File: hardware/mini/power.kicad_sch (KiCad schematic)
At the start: 33 parts, among them U1 TPS55289

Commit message: mini
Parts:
- added J2: USB_C_Receptacle_USB2.0_16P, symbol Connector:USB_C_Receptacle_USB2.0_16P
- added U7: CH224K, Package_SO:SSOP-10-1EP_3.9x4.9mm_P1mm_EP2.1x3.3mm, symbol Interface_USB:CH224K
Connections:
- new net: J2.A1 (GND), J2.A12 (GND), J2.B1 (GND), J2.B12 (GND)
- new net: J2.A4 (VBUS), J2.A9 (VBUS), J2.B4 (VBUS), J2.B9 (VBUS)
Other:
- moved on the sheet: C1, C10, C11, C12, C13, C14, C15, C16, C17, C18, C19, C2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

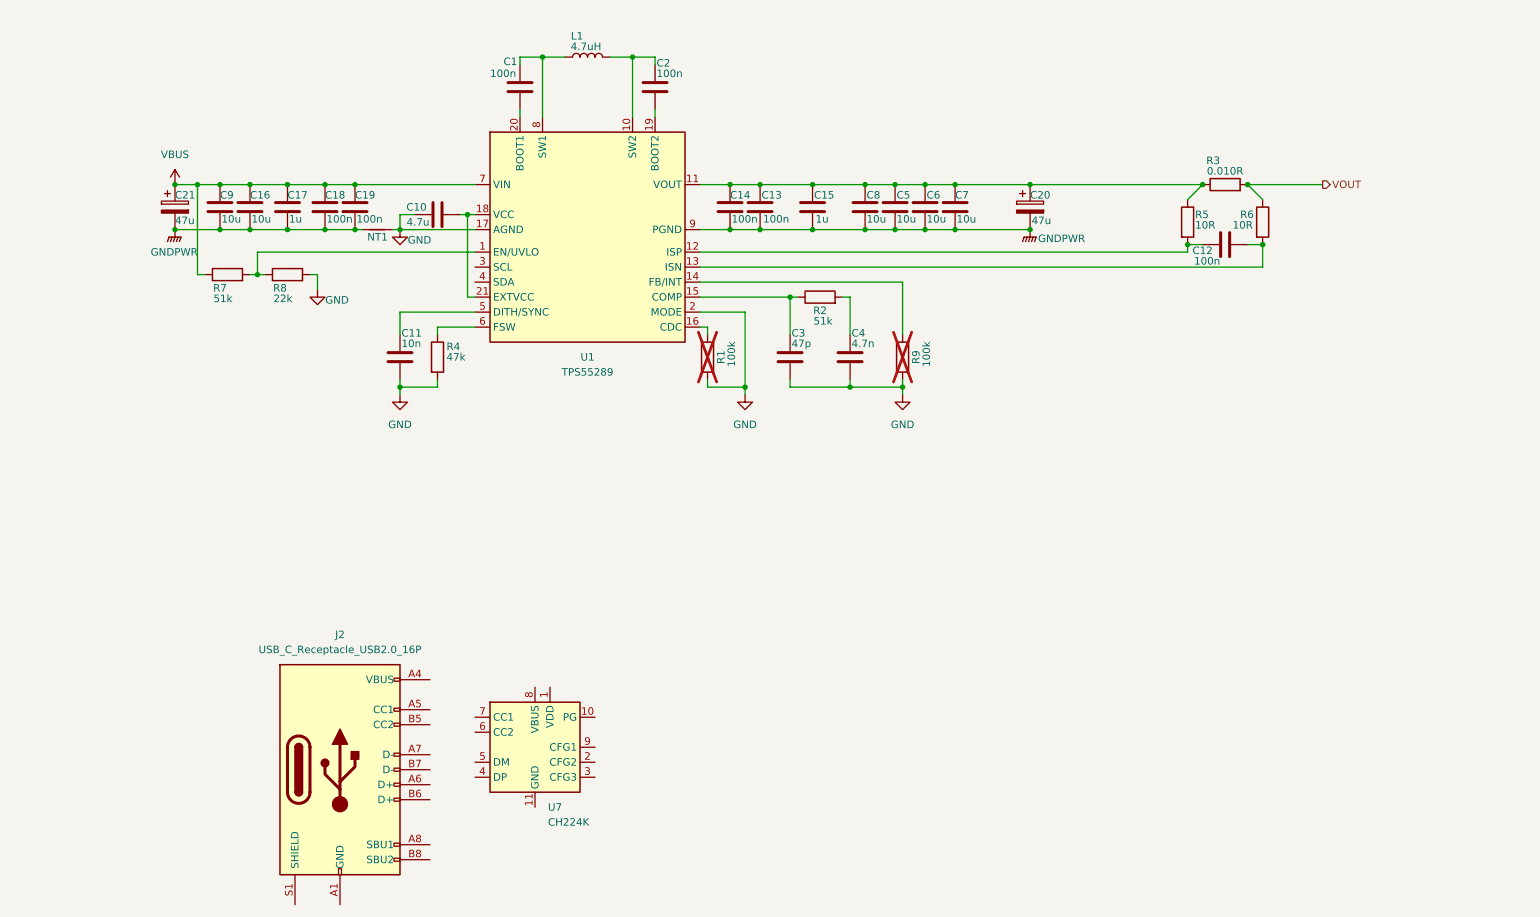
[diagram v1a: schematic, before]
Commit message: add interface & RP2040
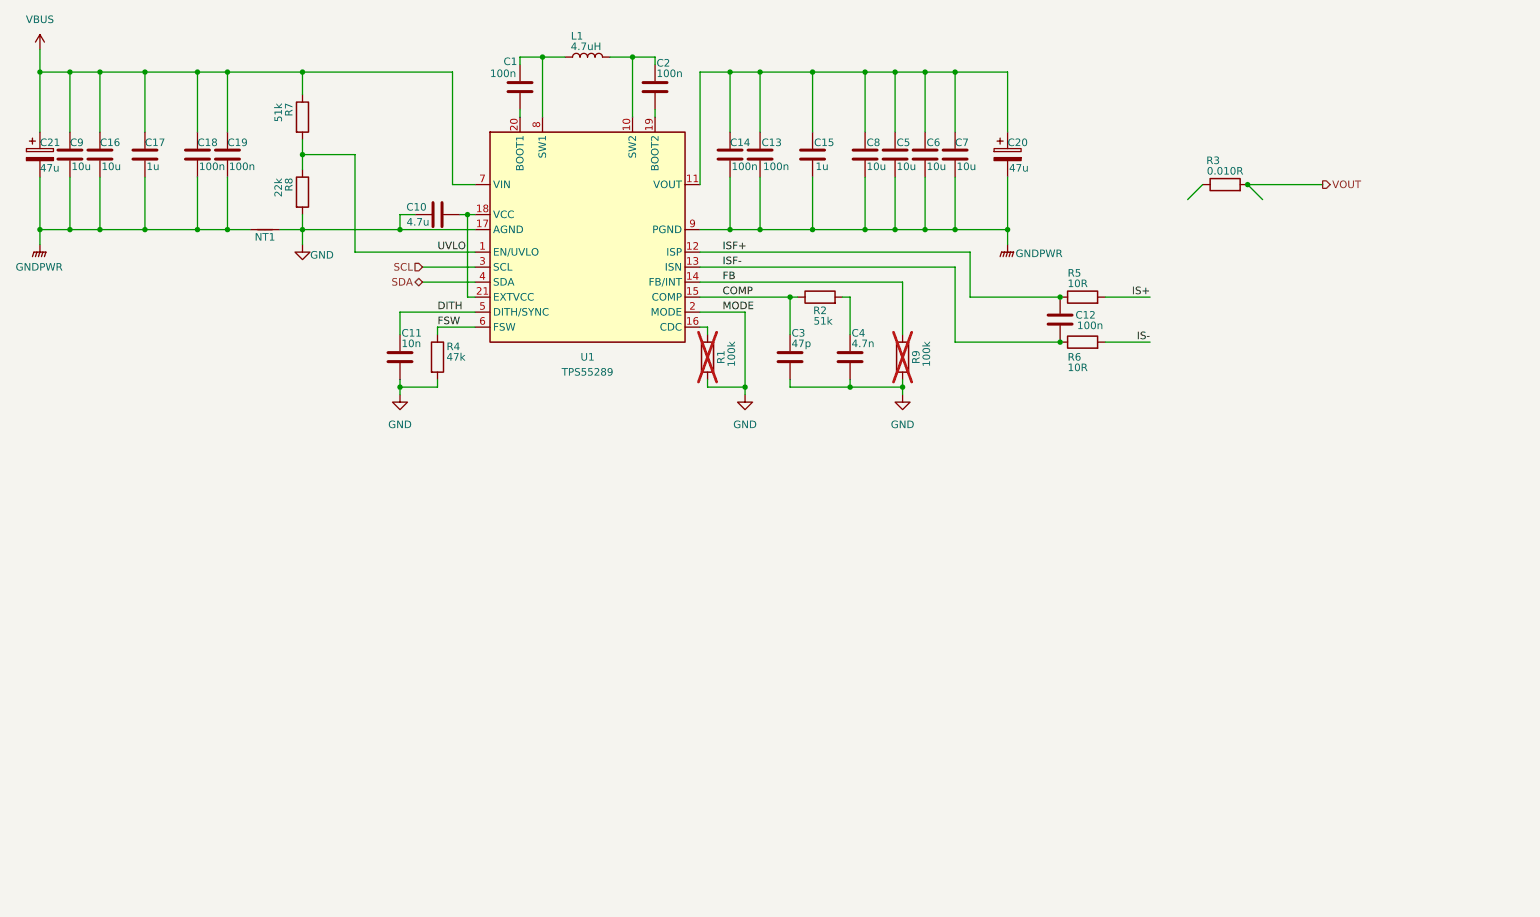
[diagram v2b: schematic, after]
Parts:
- removed J2: USB_C_Receptacle_USB2.0_16P, symbol Connector:USB_C_Receptacle_USB2.0_16P
- removed U7: CH224K, Package_SO:SSOP-10-1EP_3.9x4.9mm_P1mm_EP2.1x3.3mm, symbol Interface_USB:CH224K
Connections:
- net VOUT: no longer R6.1
- net UVLO: now reaches R7.2, R8.1, U1.1 (EN/UVLO)
- net at C13.1, C14.1, C15.1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: no longer R3.1, R5.1
- net FB: now reaches R9.2, U1.14 (FB/INT)
- net COMP: now reaches C3.1, R2.1, U1.15 (COMP)
- net SCL: now reaches U1.3 (SCL)
- net SDA: now reaches U1.4 (SDA)
- net DITH: now reaches C11.1, U1.5 (DITH/SYNC)
- net FSW: now reaches R4.1, U1.6 (FSW)
- new net IS+: R5.2
- new net IS-: R6.2
- new net ISF+: C12.2, R5.1, U1.12 (ISP)
- new net ISF-: C12.1, R6.1, U1.13 (ISN)
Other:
- moved on the sheet: C12, C13, C14, C15, C16, C17, C18, C19, C20, C21, C5, C6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

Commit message: finalize parts in schematic
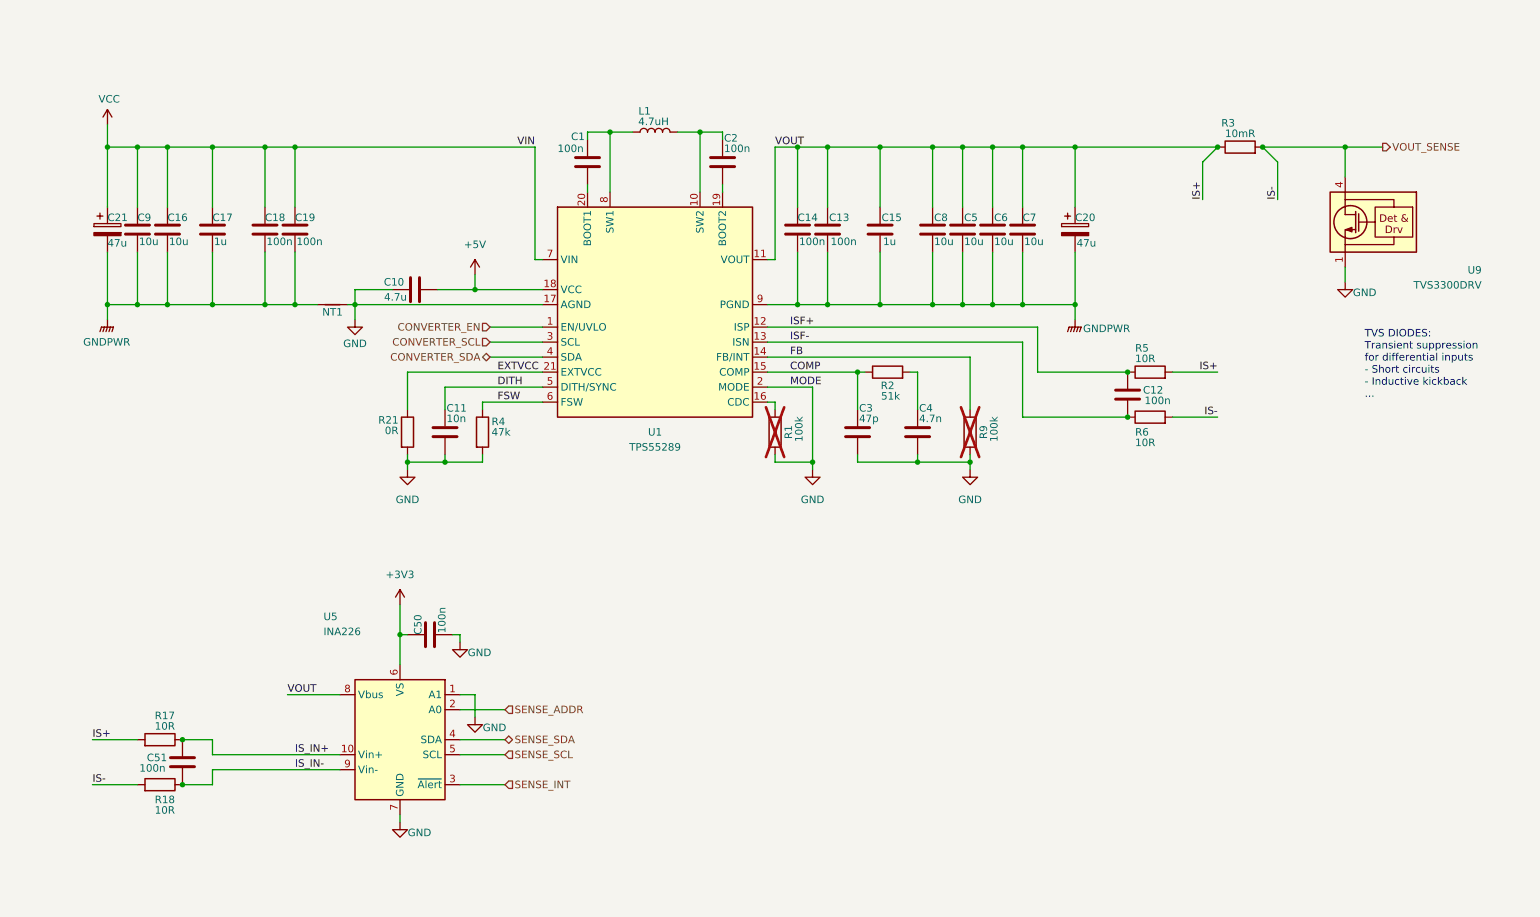
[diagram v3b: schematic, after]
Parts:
- removed R7: 51k, symbol Device:R
- removed R8: 22k, symbol Device:R
- added C50, C51: 100n, Capacitor_SMD:C_0402_1005Metric, symbol Device:C
- added R17, R18: 10R, Resistor_SMD:R_0402_1005Metric, symbol Device:R
- added R21: 0R, symbol Device:R
- added U5: INA226, Package_SO:VSSOP-10_3x3mm_P0.5mm, symbol Sensor_Energy:INA226
- added U9: TVS3300DRV, Package_SON:WSON-6-1EP_2x2mm_P0.65mm_EP1x1.6mm, symbol Power_Protection:TVS3300DRV
- R3: value 0.010R -> 10mR
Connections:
- net VOUT is gone; now on net VOUT_SENSE: R3.2
- net GND: now also C50.2, R21.2, U5.1 (A1), U5.7 (GND), U9.1 (GND), U9.2 (GND), U9.3 (GND), U9.7 (GND)
- net IS+: now also C13.1, C14.1, C15.1, C20.1, C5.1, C6.1, C7.1, C8.1, R3.1, U1.11 (VOUT), R17.2, U5.8 (Vbus)
- net +5V: now reaches C10.1, U1.18 (VCC)
- net +5V: no longer U1.21 (EXTVCC)
- net IS- renamed VOUT_SENSE
- net VOUT_SENSE: now also R18.2, U9.4 (IN), U9.5 (IN), U9.6 (IN)
- net SCL renamed CONVERTER_SCL
- net SDA renamed CONVERTER_SDA
- net UVLO renamed CONVERTER_EN
- net VBUS renamed VCC
- new net +3V3: C50.1, U5.6 (VS)
- new net EXTVCC: R21.1, U1.21 (EXTVCC)
- new net IS_IN+: C51.2, R17.1, U5.10 (Vin+)
- new net IS_IN-: C51.1, R18.1, U5.9 (Vin-)
- new net SENSE_ADDR: U5.2 (A0)
- new net SENSE_INT: U5.3 (~{Alert})
- new net SENSE_SCL: U5.5 (SCL)
- new net SENSE_SDA: U5.4 (SDA)
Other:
- note added: "TVS DIODES: Transient suppression for differential inputs - Short circuits - Inductive kickback ..."
- moved on the sheet: C1, C10, C11, C12, C13, C14, C15, C16, C17, C18, C19, C2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

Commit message: route most
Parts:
- removed NT1: NetTie_2, symbol Device:NetTie_2
- added R6: 10k, symbol Device:R
- added TH1: NTC 10k, symbol Device:Thermistor_NTC
- renumbered C21 to C1, C11 to C10, C1 to C11, C2 to C12, C14 to C13, C13 to C14, C3 to C15, C15 to C16, C4 to C17, C8 to C18, C5 to C19, C9 to C2, C6 to C20, C7 to C21, C20 to C22, C12 to C23, C16 to C3, C51 to C4, C17 to C5, C18 to C6, C19 to C7, C10 to C8, C50 to C9, R17 to R1, R6 to R10, R3 to R11, R18 to R2, R21 to R3, R1 to R5, R2 to R7, R9 to R8, R5 to R9, U5 to U1, U1 to U2, U9 to U3
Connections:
- net +3V3: now also TH1.1
- net GND: now also R6.2; no longer U2.2 (MODE)
- new net CONVERTER_ADDR: U2.2 (MODE)
- new net TEMP: R6.1, TH1.2

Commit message: ERC run
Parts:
- removed R3: 0R, symbol Device:R
- renumbered R11 to R10, R4 to R3, R5 to R4, R6 to R5, R7 to R6, R8 to R7, R9 to R8, R10 to R9
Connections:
- net EXTVCC is gone; now on net CONVERTER_VCC: U2.21 (EXTVCC)
- net +5V renamed CONVERTER_VCC

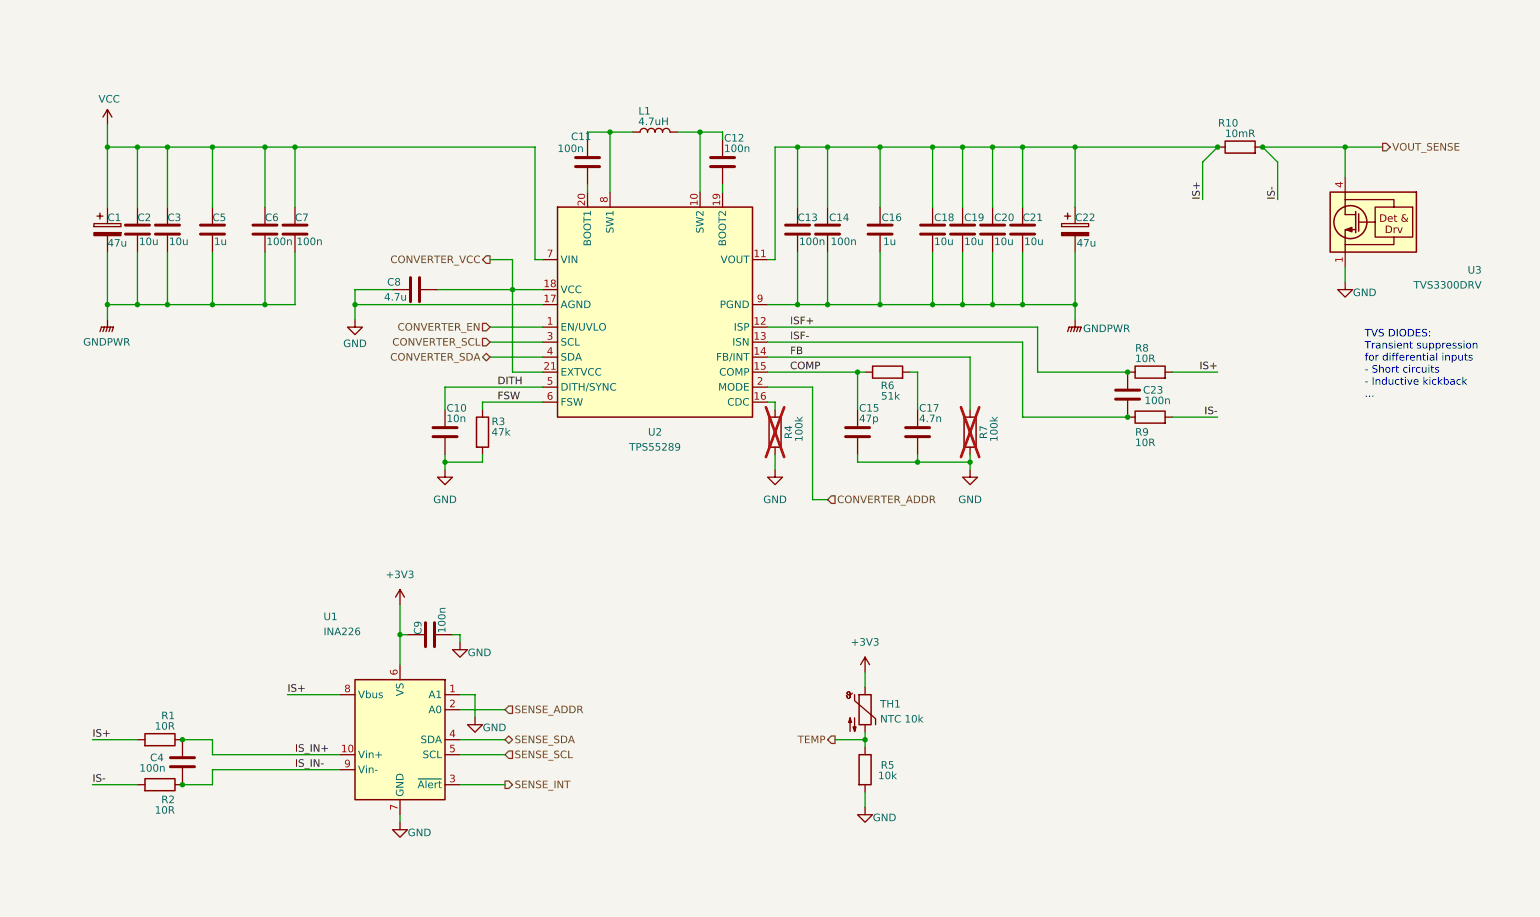
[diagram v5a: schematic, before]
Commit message: assign footprints & LCSC id
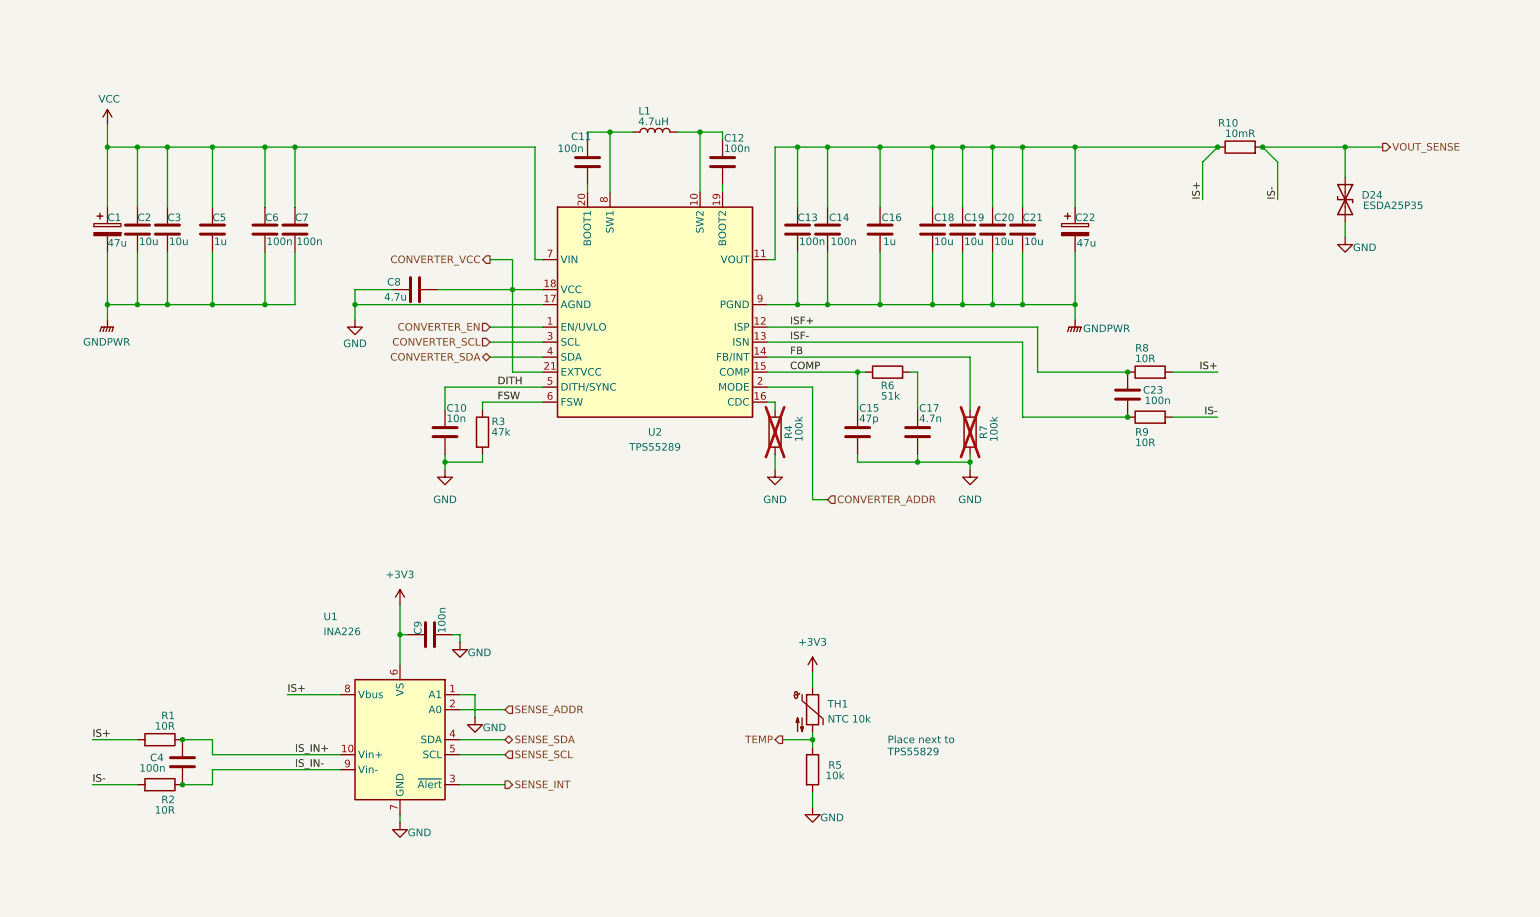
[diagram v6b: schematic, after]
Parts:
- removed U3: TVS3300DRV, Package_SON:WSON-6-1EP_2x2mm_P0.65mm_EP1x1.6mm, symbol Power_Protection:TVS3300DRV
- added D24: ESDA25P35, symbol Device:D_TVS
- C10, C15, C17: footprint (none) -> Capacitor_SMD:C_0402_1005Metric
- R10: footprint (none) -> Resistor_SMD:R_0612_1632Metric; LCSC C346837 -> C21261108
- R3, R4, R6, R7: footprint (none) -> Resistor_SMD:R_0402_1005Metric
- R5: footprint (none) -> Resistor_SMD:R_0402_1005Metric; LCSC (none) -> C25905
- TH1: footprint (none) -> Resistor_SMD:R_0402_1005Metric; LCSC (none) -> C209959
- U1: LCSC (none) -> C49851
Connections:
- net GND: now also D24.2 (A2)
- net VOUT_SENSE: now also D24.1 (A1)
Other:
- note added: "Place next to TPS55829"
- note removed: "TVS DIODES: Transient suppression for differential inputs - Short circuits - Inductive kickback ..."
- moved on the sheet: R5, TH1

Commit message: build all footprints
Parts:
- removed D24: ESDA25P35, symbol Device:D_TVS
- added C43: 10u, Capacitor_SMD:C_1206_3216Metric, symbol Device:C
- added D24: ESDA25P35, protovolt_mini_fp:D_1610_4027Metric, symbol Device:D_Zener
- added NT2: NetTie_2, symbol Device:NetTie_2
- U2: footprint (none) -> protovolt_mini_fp:Texas_RYQ0021A_VQFN-21-1EP_5x3mm_P0.5mm
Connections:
- net GND: now also NT2.2
- net GNDPWR: now also C43.2, D24.2 (A), NT2.1
- net VOUT_SENSE: now also C43.1, D24.1 (K)

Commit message: import to PCB
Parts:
- NT2: footprint (none) -> NetTie:NetTie-2_SMD_Pad0.5mm
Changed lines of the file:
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@@
 			)
 		)
-		(property "Footprint" ""
+		(property "Footprint" "NetTie:NetTie-2_SMD_Pad0.5mm"
 			(at 76.2 72.39 0)
 			(effects
